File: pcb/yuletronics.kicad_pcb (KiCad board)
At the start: 2 copper layers, 95 x 95 mm, 69 parts, among them IC1 STM32F042F6P6, IC2 MCP1700, IC3 TLV61220, J1 BATT, J2 MICROUSB, P1 SWD_TC, Q1 BSS138P, Q2 BSS138P, Q3 BSS138P, Q4 BSS138P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

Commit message: ERC/DRC
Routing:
- net /LED2: track 44.8 -> 55.2 mm
- net Net-(D1-Pad2): track 0.00 -> 2.12 mm
- net Net-(D11-Pad2): track 0.00 -> 2.00 mm
- net /LED5: track 46.1 -> 45.6 mm
- net Net-(D13-Pad1): vias 0 -> 1
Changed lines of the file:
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@@
   (general
     (links 126)
-    (no_connects 7)
+    (no_connects 0)
     (area 82.399999 62.399999 177.600001 157.600001)
     (thickness 1.6)
     (drawings 190)
-    (tracks 609)
+    (tracks 619)
     (zones 0)
     (modules 69)
@@
   (segment (start 89.95 108.85) (end 91.55 108.85) (width 0.2) (layer F.Cu) (net 9))
   (segment (start 91.55 108.85) (end 91.8 109.1) (width 0.2) (layer F.Cu) (net 9))
-  (segment (start 124.675 107.375) (end 120.675 107.375) (width 0.2) (layer F.Cu) (net 10))
+  (segment (start 124 107.2) (end 123.9 107.3) (width 0.2) (layer F.Cu) (net 10))
+  (segment (start 123.9 107.3) (end 120.6 107.3) (width 0.2) (layer F.Cu) (net 10))
+  (segment (start 124.675 107.825) (end 124.05 107.2) (width 0.2) (layer B.Cu) (net 10))
+  (segment (start 124.05 107.2) (end 124 107.2) (width 0.2) (layer B.Cu) (net 10))
+  (via (at 124 107.2) (size 0.8) (drill 0.3) (layers F.Cu B.Cu) (net 10))
   (segment (start 120.675 107.375) (end 120.6 107.3) (width 0.2) (layer F.Cu) (net 10))
   (segment (start 119.3 109.3) (end 120.6 108) (width 0.2) (layer F.Cu) (net 10))
   (segment (start 120.6 108) (end 120.6 107.3) (width 0.2) (layer F.Cu) (net 10))
   (segment (start 126.05 109.2) (end 124.675 107.825) (width 0.2) (layer B.Cu) (net 10))
-  (segment (start 124.675 107.825) (end 124.675 107.375) (width 0.2) (layer B.Cu) (net 10))
-  (via (at 124.675 107.375) (size 0.8) (drill 0.3) (layers F.Cu B.Cu) (net 10))
   (segment (start 127.325 109.6) (end 126.45 109.6) (width 0.2) (layer F.Cu) (net 10))
   (segment (start 126.45 109.6) (end 126.05 109.2) (width 0.2) (layer F.Cu) (net 10))
   (via (at 126.05 109.2) (size 0.8) (drill 0.3) (layers F.Cu B.Cu) (net 10))
-  (segment (start 133.075 109.6) (end 130.9 109.6) (width 0.2) (layer F.Cu) (net 11))
-  (segment (start 129.4 116.3) (end 125.9 119.8) (width 0.2) (layer F.Cu) (net 11))
-  (segment (start 130.9 109.6) (end 129.4 111.1) (width 0.2) (layer F.Cu) (net 11))
-  (segment (start 129.4 111.1) (end 129.4 116.3) (width 0.2) (layer F.Cu) (net 11))
+  (segment (start 129.48 116.16) (end 125.9 119.74) (width 0.2) (layer F.Cu) (net 11))
+  (segment (start 125.9 119.74) (end 125.9 119.8) (width 0.2) (layer F.Cu) (net 11))
+  (segment (start 129.48 111.88) (end 129.48 116.16) (width 0.2) (layer F.Cu) (net 11))
+  (segment (start 131.76 109.6) (end 129.48 111.88) (width 0.2) (layer F.Cu) (net 11))
+  (segment (start 133.075 109.6) (end 131.76 109.6) (width 0.2) (layer F.Cu) (net 11))
   (segment (start 125.9 119.8) (end 125.9 132.3) (width 0.2) (layer F.Cu) (net 11))
   (segment (start 126.2 135.1) (end 125.9 134.8) (width 0.2) (layer B.Cu) (net 11))
@@
   (segment (start 157.363604 138.989949) (end 158.515076 140.141421) (width 0.2) (layer F.Cu) (net 13))
   (segment (start 116.5 128.2) (end 116.8 128.2) (width 0.2) (layer F.Cu) (net 14))
-  (segment (start 116.8 128.2) (end 129 116) (width 0.2) (layer F.Cu) (net 14))
-  (segment (start 129 116) (end 129 111.7) (width 0.2) (layer F.Cu) (net 14))
-  (segment (start 128.2 110.9) (end 127.325 110.9) (width 0.2) (layer F.Cu) (net 14))
-  (segment (start 129 111.7) (end 128.2 110.9) (width 0.2) (layer F.Cu) (net 14))
+  (segment (start 116.8 128.2) (end 121.2 132.6) (width 0.2) (layer F.Cu) (net 14))
+  (segment (start 121.2 132.6) (end 123.9 132.6) (width 0.2) (layer F.Cu) (net 14))
+  (segment (start 123.9 132.6) (end 125.47 131.03) (width 0.2) (layer F.Cu) (net 14))
+  (segment (start 125.47 131.03) (end 125.47 119.54) (width 0.2) (layer F.Cu) (net 14))
+  (segment (start 125.47 119.54) (end 129.03 115.98) (width 0.2) (layer F.Cu) (net 14))
+  (segment (start 129.03 111.69) (end 128.24 110.9) (width 0.2) (layer F.Cu) (net 14))
+  (segment (start 129.03 115.98) (end 129.03 111.69) (width 0.2) (layer F.Cu) (net 14))
+  (segment (start 128.24 110.9) (end 127.325 110.9) (width 0.2) (layer F.Cu) (net 14))
   (segment (start 114.2 130.1) (end 114.6 130.1) (width 0.2) (layer B.Cu) (net 14))
   (segment (start 114.6 130.1) (end 116.5 128.2) (width 0.2) (layer B.Cu) (net 14))
@@
   (segment (start 129.3 91.975) (end 129.3 92.05) (width 0.5) (layer F.Cu) (net 18))
   (segment (start 174 110.9) (end 176 110.9) (width 0.2) (layer F.Cu) (net 19))
+  (segment (start 97.136396 75.863604) (end 98.636396 77.363604) (width 0.2) (layer F.Cu) (net 20))
   (segment (start 161.363604 142.636396) (end 162.863604 144.136396) (width 0.2) (layer F.Cu) (net 21))
   (segment (start 97.136396 75.863604) (end 98.636396 77.363604) (width 0.2) (layer B.Cu) (net 22))
@@
   (segment (start 173.75 108.85) (end 174 109.1) (width 0.2) (layer F.Cu) (net 30))
   (via (at 174 109.1) (size 0.8) (drill 0.3) (layers F.Cu B.Cu) (net 30))
+  (segment (start 100.813173 140.813173) (end 98.98995 142.636396) (width 0.2) (layer F.Cu) (net 31))
+  (via (at 98.636396 142.636396) (size 0.8) (drill 0.3) (layers F.Cu B.Cu) (net 31))
   (segment (start 98.636396 142.636396) (end 98.98995 142.636396) (width 0.2) (layer F.Cu) (net 31))
-  (segment (start 98.98995 142.636396) (end 100.813173 140.813173) (width 0.2) (layer F.Cu) (net 31))
   (segment (start 97.363604 141.363604) (end 95.863604 142.863604) (width 0.2) (layer F.Cu) (net 32))
   (segment (start 161.363604 77.363604) (end 160.936396 77.363604) (width 0.2) (layer F.Cu) (net 33))
@@
   (segment (start 86.25 111.15) (end 86 110.9) (width 0.2) (layer F.Cu) (net 35))
   (via (at 86 110.9) (size 0.8) (drill 0.3) (layers F.Cu B.Cu) (net 35))
+  (segment (start 84 109.1) (end 86 109.1) (width 0.2) (layer F.Cu) (net 36))
   (segment (start 128.85 69) (end 128.85 66.15) (width 0.2) (layer F.Cu) (net 37))
   (segment (start 128.85 66.15) (end 129 66) (width 0.2) (layer F.Cu) (net 37))

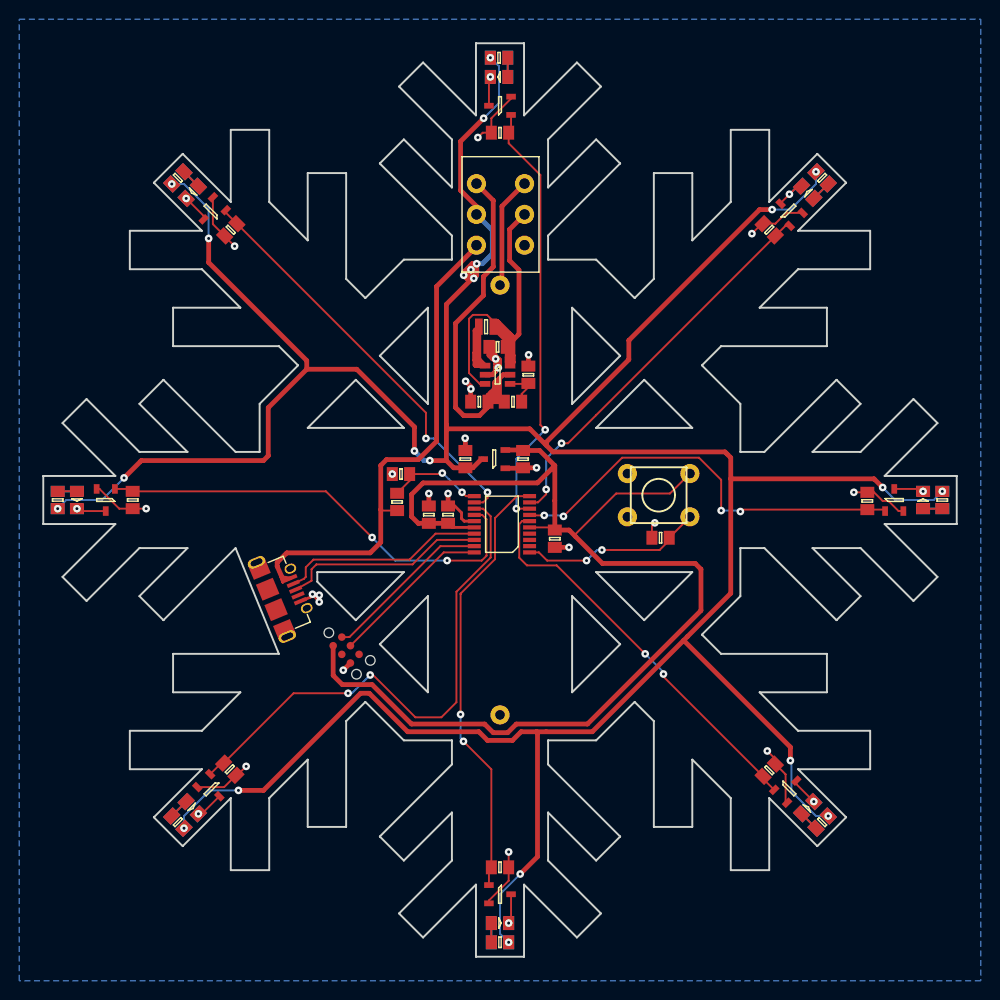
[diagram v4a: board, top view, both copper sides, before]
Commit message: Moved resistors to front, LEDs to edge
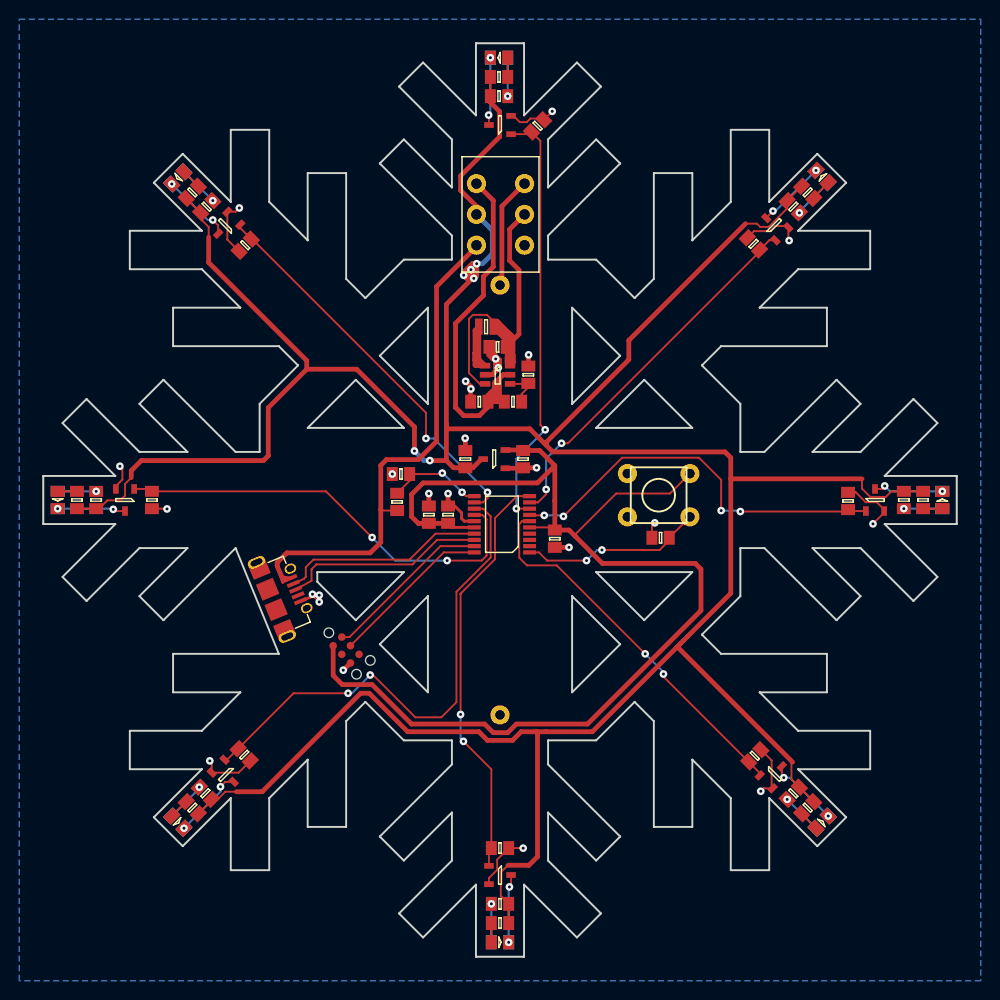
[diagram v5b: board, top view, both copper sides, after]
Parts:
- R11, R15, R17, R19, R21, R5, R7, R9: moved to F.Cu
- moved R11 4.24 mm to (160.5, 79.5)
- moved R5 4.24 mm to (99.5, 79.5)
- moved R9 4.24 mm to (160.5, 140.5)
- moved R7 4.15 mm to (99.4, 140.5)
- moved R15 4.00 mm to (130.0, 152.0)
- moved R17 4.00 mm to (88.0, 110.0)
- moved R19 4.00 mm to (172.0, 110.0)
- moved R21 4.00 mm to (129.9, 68.0)
- moved R29 3.97 mm to (133.9, 71.1), turned to 45 degrees
- moved D10 2.22 mm to (163.5, 76.4)
- moved D14 2.22 mm to (163.5, 76.4)
- moved R25 2.20 mm to (156.4, 83.4)
- moved R22 2.19 mm to (103.5, 83.5)
- moved D1 2.12 mm to (96.5, 76.5)
- moved D13 2.12 mm to (96.5, 143.5)
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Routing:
- net 5v: track 382.3 -> 365.7 mm, vias 22 -> 6
- net Net-(D2-Pad1): track 2.93 -> 7.55 mm, vias 1 -> 2
- net Net-(D13-Pad1): track 2.93 -> 7.54 mm, vias 1 -> 2
- net Net-(D1-Pad1): track 2.93 -> 7.48 mm, vias 1 -> 2
- net Net-(D4-Pad1): track 3.10 -> 7.36 mm, vias 1 -> 2
- net Net-(D3-Pad1): track 3.10 -> 7.10 mm, vias 1 -> 2
- net Net-(D11-Pad1): track 3.10 -> 7.10 mm, vias 1 -> 2
- net Net-(D12-Pad1): track 3.27 -> 7.09 mm, vias 1 -> 2
- net GND: track 83.9 -> 81.2 mm, vias 24 -> 25
- net Net-(D10-Pad1): track 4.59 -> 7.25 mm, vias 1 -> 2
- net Net-(D14-Pad2): track 2.12 -> 4.38 mm, vias 0 -> 1
- net Net-(D6-Pad2): track 2.12 -> 4.24 mm, vias 0 -> 1
- net Net-(D5-Pad2): track 2.12 -> 4.24 mm, vias 0 -> 1
- net /LED3: track 41.6 -> 39.5 mm
- net /LED2: track 55.2 -> 53.1 mm
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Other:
- board text added: "2016-11-07"
- board text added: "DAVID TURNER"
